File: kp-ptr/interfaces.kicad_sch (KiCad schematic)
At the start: 2 parts

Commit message: LIS + SDCARD Signed-off-by: kretu <krecik@gmail.com>
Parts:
- added J?: Micro_SD_Card_Det, symbol Connector:Micro_SD_Card_Det
- added R? (x7): 50k, symbol Device:R
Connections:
- net Earth: now also J?.11 (SHIELD), J?.6 (VSS)
- new net: J?.4 (VDD), R?.1
- new net: J?.8 (DAT1), R?.1
- new net: J?.1 (DAT2), R?.1
- new net +3V3: R?.2, R?.2, R?.2, R?.2, R?.2, R?.2, R?.2
- new net SPI_CLK: J?.5 (CLK), R?.1
- new net SPI_CS_SDCARD: J?.2 (DAT3/CD), R?.1
- new net SPI_MISO: J?.7 (DAT0), R?.1
- new net SPI_MOSI: J?.3 (CMD), R?.1

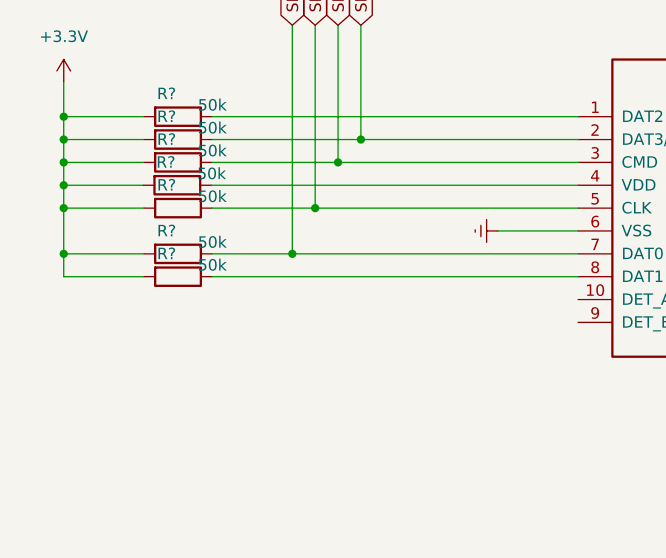
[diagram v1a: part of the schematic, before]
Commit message: poprawiony babol przy sd Signed-off-by: kretu <krecik@gmail.com>
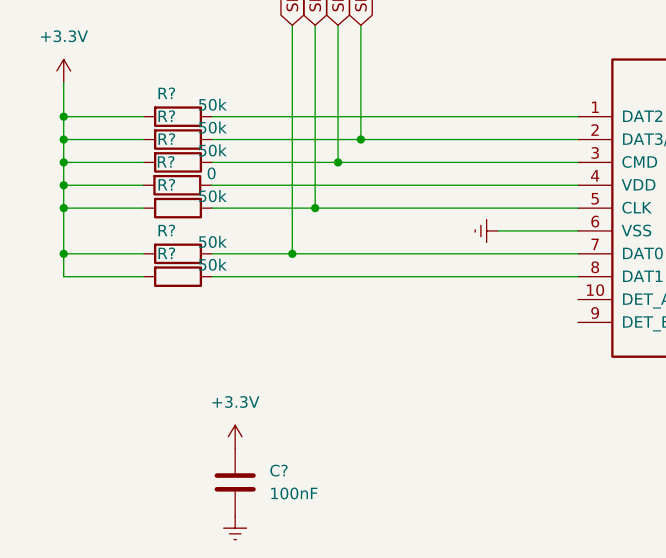
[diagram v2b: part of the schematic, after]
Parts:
- added C?: 100nF, symbol Device:C
- R?: value 50k -> 0
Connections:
- net +3V3: now also C?.1
- net Earth: now also C?.2
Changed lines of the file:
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@@
     (in_bom yes) (on_board yes)
     (property "Reference" "R?" (id 0) (at 68.5041 100.33 90))
-    (property "Value" "50k" (id 1) (at 73.5841 101.6 90))
+    (property "Value" "0" (id 1) (at 73.5841 101.6 90))
     (property "Footprint" "" (id 2) (at 69.7741 101.092 90)
       (effects (font (size 1.27 1.27)) hide)
@@
     (pin "1")
     (pin "2")
+  )
+  (symbol (lib_id "power:+3.3V") (at 76.2 132.08 0) (unit 1)
+    (in_bom yes) (on_board yes) (fields_autoplaced)
+    (property "Reference" "#PWR?" (id 0) (at 76.2 135.89 0)
+      (effects (font (size 1.27 1.27)) hide)
+    )
+    (property "Value" "+3.3V" (id 1) (at 76.2 127 0))
+    (property "Footprint" "" (id 2) (at 76.2 132.08 0)
+      (effects (font (size 1.27 1.27)) hide)
+    )
+    (property "Datasheet" "" (id 3) (at 76.2 132.08 0)
+      (effects (font (size 1.27 1.27)) hide)
+    )
+    (pin "1")
   )
   (symbol (lib_id "power:Earth") (at 96.52 36.83 0) (unit 1)
@@
     (pin "S1")
   )
+  (symbol (lib_id "Device:C") (at 76.2 135.89 0) (unit 1)
+    (in_bom yes) (on_board yes) (fields_autoplaced)
+    (property "Reference" "C?" (id 0) (at 80.01 134.6199 0)
+      (effects (font (size 1.27 1.27)) (justify left))
+    )
+    (property "Value" "100nF" (id 1) (at 80.01 137.1599 0)
+      (effects (font (size 1.27 1.27)) (justify left))
+    )
+    (property "Footprint" "" (id 2) (at 77.1652 139.7 0)
+      (effects (font (size 1.27 1.27)) hide)
+    )
+    (property "Datasheet" "~" (id 3) (at 76.2 135.89 0)
+      (effects (font (size 1.27 1.27)) hide)
+    )
+    (pin "1")
+    (pin "2")
+  )
+  (symbol (lib_id "power:Earth") (at 76.2 139.7 0) (unit 1)
+    (in_bom yes) (on_board yes) (fields_autoplaced)
+    (property "Reference" "#PWR?" (id 0) (at 76.2 146.05 0)
+      (effects (font (size 1.27 1.27)) hide)
+    )
+    (property "Value" "Earth" (id 1) (at 76.2 143.51 0)
+      (effects (font (size 1.27 1.27)) hide)
+    )
+    (property "Footprint" "" (id 2) (at 76.2 139.7 0)
+      (effects (font (size 1.27 1.27)) hide)
+    )
+    (property "Datasheet" "~" (id 3) (at 76.2 139.7 0)
+      (effects (font (size 1.27 1.27)) hide)
+    )
+    (pin "1")
+  )
 )

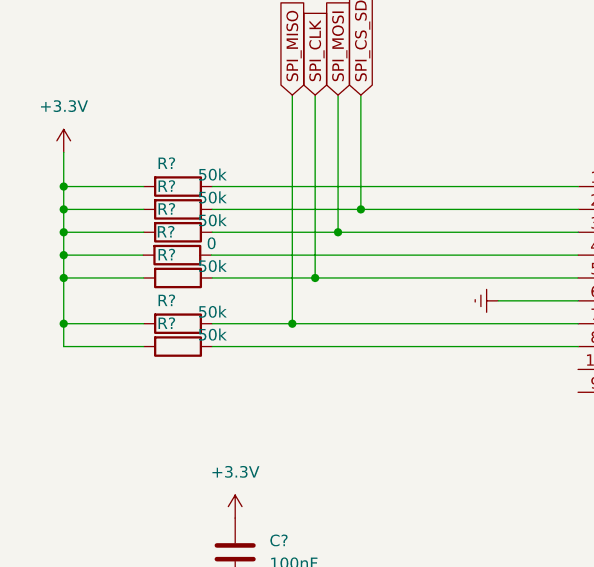
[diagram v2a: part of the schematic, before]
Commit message: SD bez pullupa na CLK jak w gotowym układzie od ST
Signed-off-by: kretu <krecik@gmail.com>
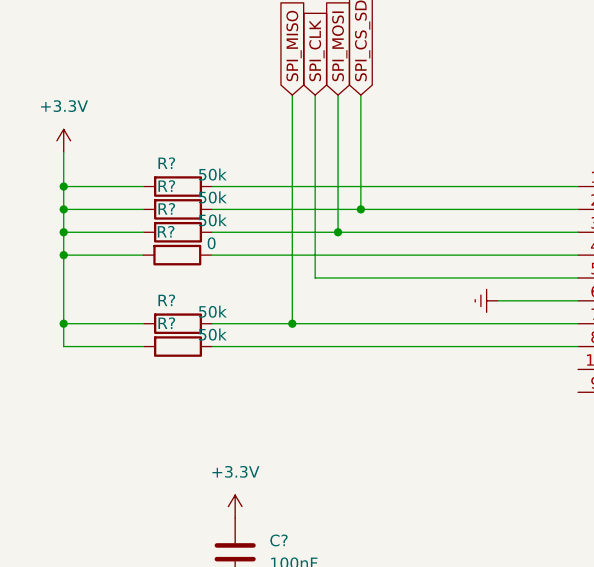
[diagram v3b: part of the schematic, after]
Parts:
- removed R?: 50k, symbol Device:R
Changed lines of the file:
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@@
   (junction (at 87.63 100.33) (diameter 0) (color 0 0 0 0)
   )
-  (junction (at 57.15 105.41) (diameter 0) (color 0 0 0 0)
-  )
   (junction (at 57.15 95.25) (diameter 0) (color 0 0 0 0)
   )
   (junction (at 115.57 35.56) (diameter 0) (color 0 0 0 0)
   )
-  (junction (at 85.09 105.41) (diameter 0) (color 0 0 0 0)
-  )
   (junction (at 115.57 38.1) (diameter 0) (color 0 0 0 0)
   )
@@
     (stroke (width 0) (type default) (color 0 0 0 0))
   )
-  (wire (pts (xy 57.15 105.41) (xy 66.04 105.41))
-    (stroke (width 0) (type default) (color 0 0 0 0))
-  )
   (wire (pts (xy 57.15 102.87) (xy 57.15 100.33))
     (stroke (width 0) (type default) (color 0 0 0 0))
@@
     (stroke (width 0) (type default) (color 0 0 0 0))
   )
-  (wire (pts (xy 57.15 110.49) (xy 57.15 105.41))
+  (wire (pts (xy 57.15 102.87) (xy 57.15 110.49))
     (stroke (width 0) (type default) (color 0 0 0 0))
   )
@@
     (stroke (width 0) (type default) (color 0 0 0 0))
   )
-  (wire (pts (xy 73.66 105.41) (xy 85.09 105.41))
-    (stroke (width 0) (type default) (color 0 0 0 0))
-  )
   (wire (pts (xy 114.3 105.41) (xy 85.09 105.41))
     (stroke (width 0) (type default) (color 0 0 0 0))
@@
   )
   (wire (pts (xy 66.04 113.03) (xy 57.15 113.03))
-    (stroke (width 0) (type default) (color 0 0 0 0))
-  )
-  (wire (pts (xy 57.15 105.41) (xy 57.15 102.87))
     (stroke (width 0) (type default) (color 0 0 0 0))
   )
@@
     (pin "1")
   )
-  (symbol (lib_id "Device:R") (at 69.85 105.41 270) (unit 1)
-    (in_bom yes) (on_board yes)
-    (property "Reference" "R?" (id 0) (at 68.58 102.87 90))
-    (property "Value" "50k" (id 1) (at 73.66 104.14 90))
-    (property "Footprint" "" (id 2) (at 69.85 103.632 90)
-      (effects (font (size 1.27 1.27)) hide)
-    )
-    (property "Datasheet" "~" (id 3) (at 69.85 105.41 0)
-      (effects (font (size 1.27 1.27)) hide)
-    )
-    (pin "1")
-    (pin "2")
-  )
   (symbol (lib_id "power:VBUS") (at 73.66 36.83 0) (unit 1)

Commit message: GPS lora wrzucone symbole Signed-off-by: kretu <krecik@gmail.com>
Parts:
- added C?: ???, symbol Device:C
- added IC?: E22-900M22S, E22-900M22S, symbol KP-PTR_lib:E22-900M22S
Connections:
- net +3V3: now also C?.1, IC?.9 (VCC)
- net Earth: now also C?.2, IC?.1 (GND), IC?.10 (GND), IC?.11 (GND), IC?.12 (GND), IC?.2 (GND), IC?.20 (GND), IC?.22 (GND), IC?.3 (GND), IC?.4 (GND), IC?.5 (GND)
- net SPI_CLK: now also IC?.18 (SCK)
- net SPI_MISO: now also IC?.16 (MISO)
- net SPI_MOSI: now also IC?.17 (MOSI)
- new net SPI_CS_LORA: IC?.19 (NSS)
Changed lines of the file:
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@@
   (junction (at 57.15 110.49) (diameter 0) (color 0 0 0 0)
   )
+  (wire (pts (xy 222.25 33.02) (xy 222.25 36.83))
+    (stroke (width 0) (type default) (color 0 0 0 0))
+  )
   (wire (pts (xy 57.15 97.79) (xy 66.04 97.79))
     (stroke (width 0) (type default) (color 0 0 0 0))
@@
     (stroke (width 0) (type default) (color 0 0 0 0))
   )
+  (wire (pts (xy 204.47 46.99) (xy 209.55 46.99))
+    (stroke (width 0) (type default) (color 0 0 0 0))
+  )
   (wire (pts (xy 68.58 38.1) (xy 63.5 38.1))
     (stroke (width 0) (type default) (color 0 0 0 0))
@@
     (stroke (width 0) (type default) (color 0 0 0 0))
   )
+  (wire (pts (xy 222.25 72.39) (xy 222.25 67.31))
+    (stroke (width 0) (type default) (color 0 0 0 0))
+  )
   (wire (pts (xy 57.15 102.87) (xy 57.15 100.33))
     (stroke (width 0) (type default) (color 0 0 0 0))
@@
     (stroke (width 0) (type default) (color 0 0 0 0))
   )
+  (wire (pts (xy 204.47 41.91) (xy 209.55 41.91))
+    (stroke (width 0) (type default) (color 0 0 0 0))
+  )
   (wire (pts (xy 105.41 107.95) (xy 114.3 107.95))
     (stroke (width 0) (type default) (color 0 0 0 0))
@@
     (stroke (width 0) (type default) (color 0 0 0 0))
   )
+  (wire (pts (xy 204.47 49.53) (xy 209.55 49.53))
+    (stroke (width 0) (type default) (color 0 0 0 0))
+  )
   (wire (pts (xy 109.22 46.99) (xy 109.22 38.1))
     (stroke (width 0) (type default) (color 0 0 0 0))
@@
   )
   (wire (pts (xy 83.82 46.99) (xy 68.58 46.99))
+    (stroke (width 0) (type default) (color 0 0 0 0))
+  )
+  (wire (pts (xy 204.47 44.45) (xy 209.55 44.45))
     (stroke (width 0) (type default) (color 0 0 0 0))
   )
@@
     )
   )
+  (global_label "SPI_CLK" (shape input) (at 204.47 44.45 180) (fields_autoplaced)
+    (effects (font (size 1.27 1.27)) (justify right))
+    (property "Intersheet References" "${INTERSHEET_REFS}" (id 0) (at 194.4369 44.3706 0)
+      (effects (font (size 1.27 1.27)) (justify right) hide)
+    )
+  )
   (global_label "SPI_MOSI" (shape input) (at 87.63 85.09 90) (fields_autoplaced)
     (effects (font (size 1.27 1.27)) (justify left))
@@
     )
   )
+  (global_label "SPI_CS_LORA" (shape input) (at 204.47 41.91 180) (fields_autoplaced)
+    (effects (font (size 1.27 1.27)) (justify right))
+    (property "Intersheet References" "${INTERSHEET_REFS}" (id 0) (at 189.8407 41.8306 0)
+      (effects (font (size 1.27 1.27)) (justify right) hide)
+    )
+  )
   (global_label "SPI_CS_SDCARD" (shape input) (at 90.17 85.09 90) (fields_autoplaced)
     (effects (font (size 1.27 1.27)) (justify left))
     (property "Intersheet References" "${INTERSHEET_REFS}" (id 0) (at 90.2494 67.7998 90)
       (effects (font (size 1.27 1.27)) (justify left) hide)
+    )
+  )
+  (global_label "SPI_MOSI" (shape input) (at 204.47 46.99 180) (fields_autoplaced)
+    (effects (font (size 1.27 1.27)) (justify right))
+    (property "Intersheet References" "${INTERSHEET_REFS}" (id 0) (at 193.4088 46.9106 0)
+      (effects (font (size 1.27 1.27)) (justify right) hide)
+    )
+  )
+  (global_label "SPI_MISO" (shape input) (at 204.47 49.53 180) (fields_autoplaced)
+    (effects (font (size 1.27 1.27)) (justify right))
+    (property "Intersheet References" "${INTERSHEET_REFS}" (id 0) (at 193.4088 49.4506 0)
+      (effects (font (size 1.27 1.27)) (justify right) hide)
     )
   )
@@
     (pin "1")
   )
+  (symbol (lib_id "power:Earth") (at 234.95 85.09 0) (unit 1)
+    (in_bom yes) (on_board yes) (fields_autoplaced)
+    (property "Reference" "#PWR?" (id 0) (at 234.95 91.44 0)
+      (effects (font (size 1.27 1.27)) hide)
+    )
+    (property "Value" "Earth" (id 1) (at 234.95 88.9 0)
+      (effects (font (size 1.27 1.27)) hide)
+    )
+    (property "Footprint" "" (id 2) (at 234.95 85.09 0)
+      (effects (font (size 1.27 1.27)) hide)
+    )
+    (property "Datasheet" "~" (id 3) (at 234.95 85.09 0)
+      (effects (font (size 1.27 1.27)) hide)
+    )
+    (pin "1")
+  )
   (symbol (lib_id "power:Earth") (at 138.43 58.42 0) (unit 1)
     (in_bom yes) (on_board yes) (fields_autoplaced)
@@
     )
     (property "Datasheet" "~" (id 3) (at 138.43 58.42 0)
+      (effects (font (size 1.27 1.27)) hide)
+    )
+    (pin "1")
+  )
+  (symbol (lib_id "power:Earth") (at 222.25 72.39 0) (unit 1)
+    (in_bom yes) (on_board yes) (fields_autoplaced)
+    (property "Reference" "#PWR?" (id 0) (at 222.25 78.74 0)
+      (effects (font (size 1.27 1.27)) hide)
+    )
+    (property "Value" "Earth" (id 1) (at 222.25 76.2 0)
+      (effects (font (size 1.27 1.27)) hide)
+    )
+    (property "Footprint" "" (id 2) (at 222.25 72.39 0)
+      (effects (font (size 1.27 1.27)) hide)
+    )
+    (property "Datasheet" "~" (id 3) (at 222.25 72.39 0)
       (effects (font (size 1.27 1.27)) hide)
     )
@@
     (pin "2")
   )
+  (symbol (lib_id "power:+3.3V") (at 234.95 77.47 0) (unit 1)
+    (in_bom yes) (on_board yes) (fields_autoplaced)
+    (property "Reference" "#PWR?" (id 0) (at 234.95 81.28 0)
+      (effects (font (size 1.27 1.27)) hide)
+    )
+    (property "Value" "+3.3V" (id 1) (at 234.95 72.39 0))
+    (property "Footprint" "" (id 2) (at 234.95 77.47 0)
+      (effects (font (size 1.27 1.27)) hide)
+    )
+    (property "Datasheet" "" (id 3) (at 234.95 77.47 0)
+      (effects (font (size 1.27 1.27)) hide)
+    )
+    (pin "1")
+  )
   (symbol (lib_id "power:Earth") (at 130.81 58.42 0) (unit 1)
     (in_bom yes) (on_board yes) (fields_autoplaced)
@@
     )
     (pin "1")
+  )
+  (symbol (lib_id "Device:C") (at 234.95 81.28 0) (unit 1)
+    (in_bom yes) (on_board yes) (fields_autoplaced)
+    (property "Reference" "C?" (id 0) (at 238.76 80.0099 0)
+      (effects (font (size 1.27 1.27)) (justify left))
+    )
+    (property "Value" "???" (id 1) (at 238.76 82.5499 0)
+      (effects (font (size 1.27 1.27)) (justify left))
+    )
+    (property "Footprint" "" (id 2) (at 235.9152 85.09 0)
+      (effects (font (size 1.27 1.27)) hide)
+    )
+    (property "Datasheet" "~" (id 3) (at 234.95 81.28 0)
+      (effects (font (size 1.27 1.27)) hide)
+    )
+    (pin "1")
+    (pin "2")
+  )
+  (symbol (lib_id "KP-PTR_lib:E22-900M22S") (at 222.25 52.07 0) (unit 1)
+    (in_bom yes) (on_board yes) (fields_autoplaced)
+    (property "Reference" "IC?" (id 0) (at 224.1297 34.29 0)
+      (effects (font (size 1.27 1.27)) (justify left))
+    )
+    (property "Value" "E22-900M22S" (id 1) (at 224.1297 36.83 0)
+      (effects (font (size 1.27 1.27)) (justify left))
+    )
+    (property "Footprint" "E22-900M22S" (id 2) (at 222.25 52.07 0)
+      (effects (font (size 1.27 1.27)) (justify left bottom) hide)
+    )
+    (property "Datasheet" "" (id 3) (at 222.25 52.07 0)
+      (effects (font (size 1.27 1.27)) (justify left bottom) hide)
+    )
+    (pin "1")
+    (pin "10")
+    (pin "11")
+    (pin "12")
+    (pin "13")
+    (pin "14")
+    (pin "15")
+    (pin "16")
+    (pin "17")
+    (pin "18")
+    (pin "19")
+    (pin "2")
+    (pin "20")
+    (pin "21")
+    (pin "22")
+    (pin "3")
+    (pin "4")
+    (pin "5")
+    (pin "6")
+    (pin "7")
+    (pin "8")
+    (pin "9")
   )
   (symbol (lib_id "power:VBUS") (at 73.66 36.83 0) (unit 1)
@@
     (pin "2")
   )
+  (symbol (lib_id "power:+3.3V") (at 222.25 33.02 0) (unit 1)
+    (in_bom yes) (on_board yes) (fields_autoplaced)
+    (property "Reference" "#PWR?" (id 0) (at 222.25 36.83 0)
+      (effects (font (size 1.27 1.27)) hide)
+    )
+    (property "Value" "+3.3V" (id 1) (at 222.25 27.94 0))
+    (property "Footprint" "" (id 2) (at 222.25 33.02 0)
+      (effects (font (size 1.27 1.27)) hide)
+    )
+    (property "Datasheet" "" (id 3) (at 222.25 33.02 0)
+      (effects (font (size 1.27 1.27)) hide)
+    )
+    (pin "1")
+  )
   (symbol (lib_id "power:+3.3V") (at 57.15 91.44 0) (unit 1)

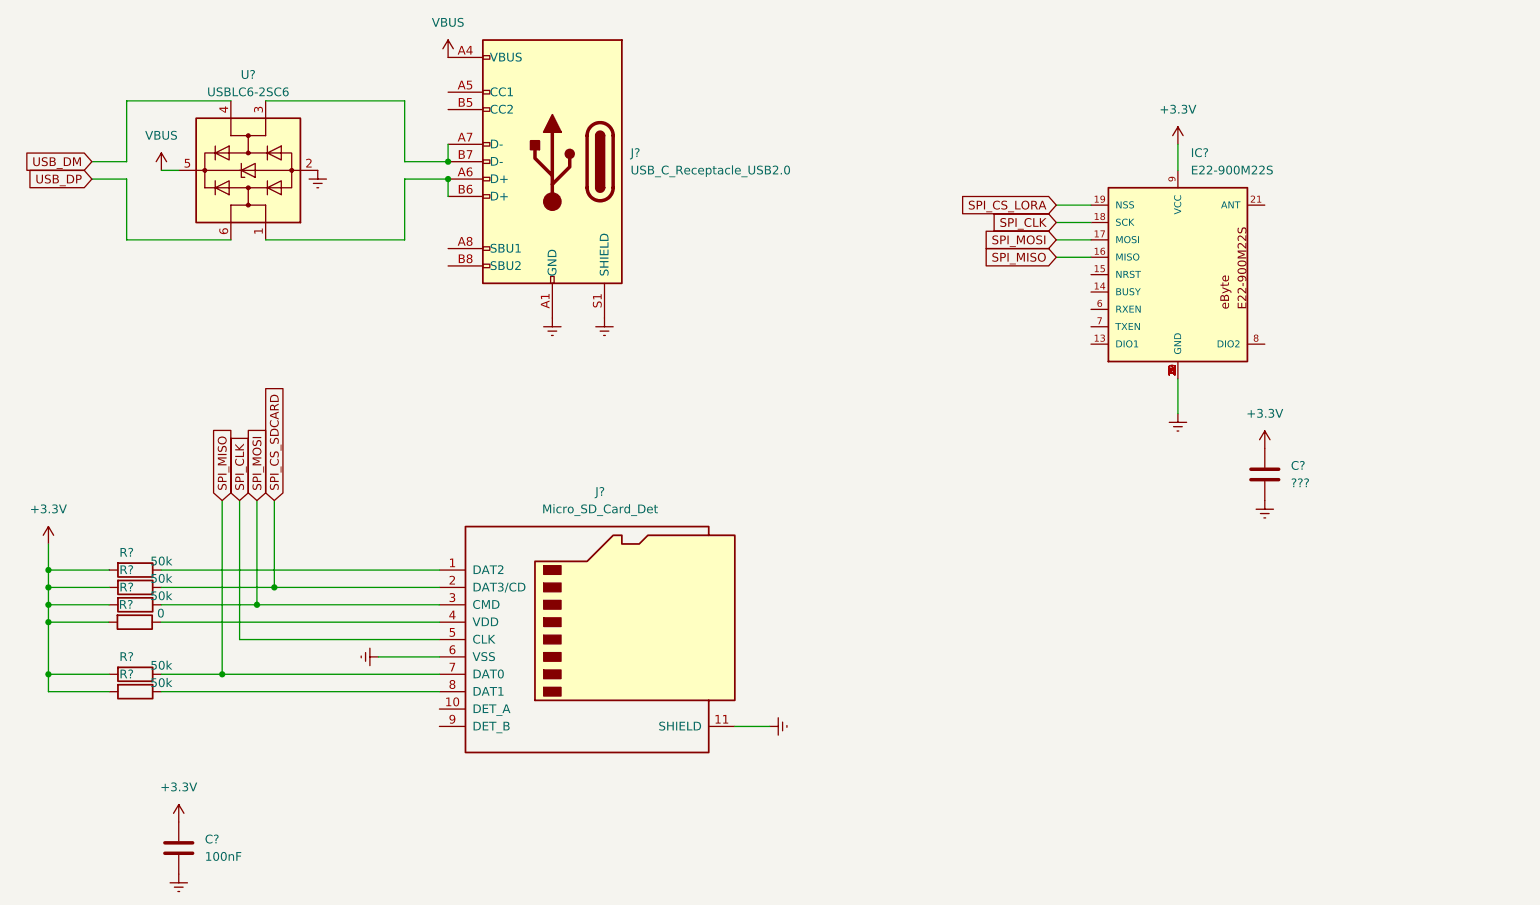
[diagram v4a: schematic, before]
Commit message: Footprints IN IMU9DOF OUT Signed-off-by: kretu <krecik@gmail.com>
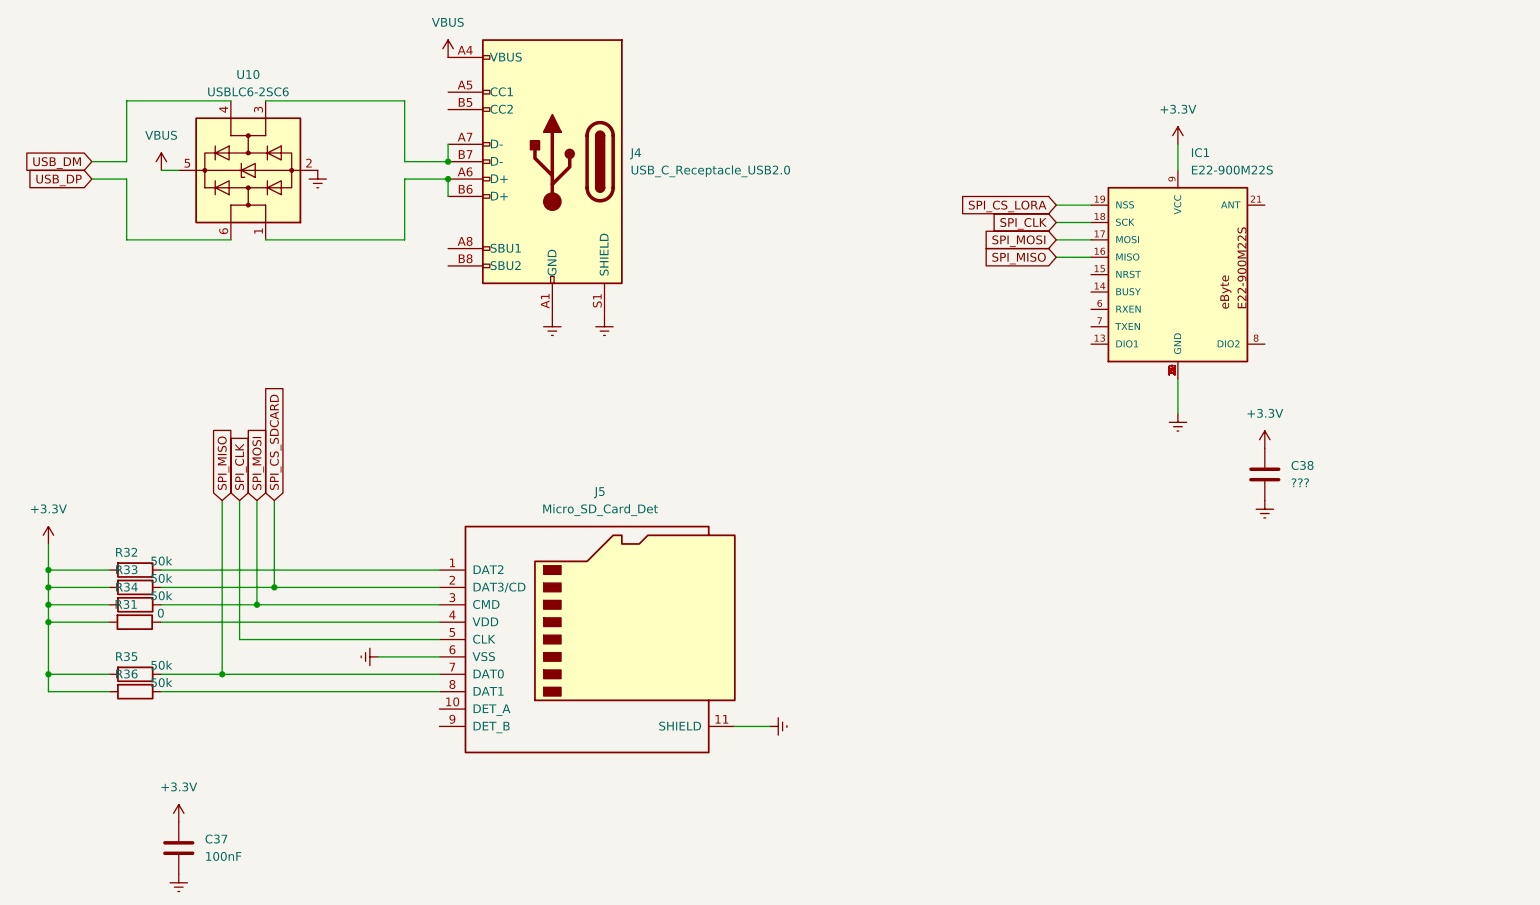
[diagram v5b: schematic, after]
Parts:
- C37, C38: renamed from C?; footprint (none) -> Capacitor_SMD:C_01005_0402Metric_Pad0.57x0.30mm_HandSolder
- IC1: renamed from IC?; footprint E22-900M22S -> KP-PTR_lib:E22-900M22S
- J4: renamed from J?; footprint (none) -> KP-PTR_lib:217B-BC02
- R31, R32, R33, R34, R35, R36: renamed from R?; footprint (none) -> Resistor_SMD:R_0402_1005Metric_Pad0.72x0.64mm_HandSolder
- gave numbers to parts that had none: 2
